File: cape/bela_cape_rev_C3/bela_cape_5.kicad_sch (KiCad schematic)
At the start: 28 parts, among them IC2 TLV320AIC3104, IC3 MIC5317

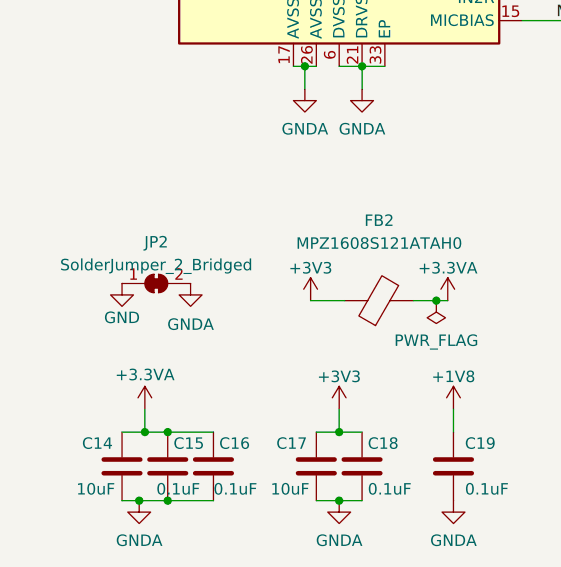
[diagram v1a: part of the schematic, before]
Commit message: removed sym-lib-table with a reference to an unused and obsolete local library
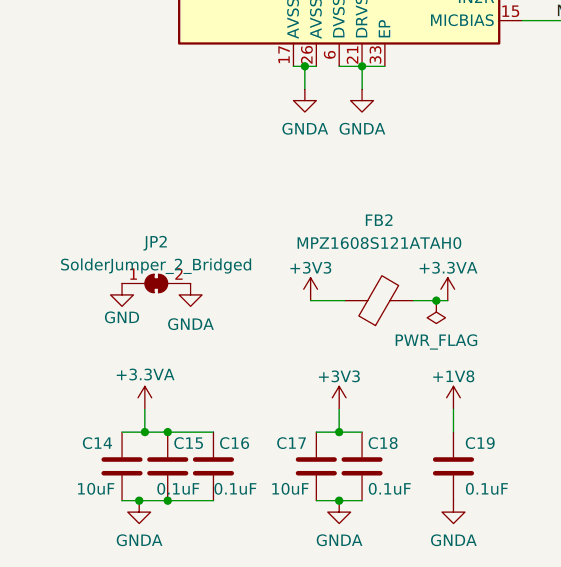
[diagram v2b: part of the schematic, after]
